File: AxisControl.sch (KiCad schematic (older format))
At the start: 0 parts

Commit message: Added the rest of the printer parts. Should be complete more or less.
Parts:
- added J5: Max, symbol Connector_Generic:Conn_02x01
- added J6: Min, symbol Connector_Generic:Conn_02x01
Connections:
- new net GND: J5.2 (Pin_2), J6.2 (Pin_2)
- new net MaxStop/SENSOR: J5.1 (Pin_1)
- new net MinStop/SENSOR: J6.1 (Pin_1)
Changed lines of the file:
@@
 EESchema Schematic File Version 4
+LIBS:PrntrBoardV1-cache
 EELAYER 26 0
 EELAYER END
 $Descr A4 11693 8268
 encoding utf-8
-Sheet 8 29
+Sheet 8 35
 Title ""
 Date ""
@@
 	5150 4000 5150 3300
 Connection ~ 5150 3300
-Text HLabel 6150 3350 2    50   Input ~ 0
-MAXSTOP
 Text HLabel 6150 3500 2    50   Output ~ 0
 MAXSTOP_OUT
 Text HLabel 6150 4150 2    50   Output ~ 0
 MINSTOP_OUT
-Text HLabel 6150 4000 2    50   Input ~ 0
-MINSTOP
-Wire Wire Line
-	6050 4000 6150 4000
 Wire Wire Line
 	6050 4150 6150 4150
 Wire Wire Line
 	6050 3500 6150 3500
-Wire Wire Line
-	6050 3350 6150 3350
+$Comp
+L Connector_Generic:Conn_02x01 J5
+U 1 1 5AE0BB35
+P 6450 3350
+AR Path="/5AC337B6/5ACC0AA2/5AE0BB35" Ref="J5"  Part="1"
+AR Path="/5AC337B6/5ACCA309/5AE0BB35" Ref="J7"  Part="1"
+AR Path="/5AC337B6/5ACE1C6D/5AE0BB35" Ref="J9"  Part="1"
+F 0 "J9" H 6500 3567 50  0000 C CNN
+F 1 "Max" H 6500 3476 50  0000 C CNN
+F 2 "" H 6450 3350 50  0001 C CNN
+F 3 "~" H 6450 3350 50  0001 C CNN
+	1    6450 3350
+	1    0    0    -1
+$EndComp
+$Comp
+L Connector_Generic:Conn_02x01 J6
+U 1 1 5AE0BBC2
+P 6450 4000
+AR Path="/5AC337B6/5ACC0AA2/5AE0BBC2" Ref="J6"  Part="1"
+AR Path="/5AC337B6/5ACCA309/5AE0BBC2" Ref="J8"  Part="1"
+AR Path="/5AC337B6/5ACE1C6D/5AE0BBC2" Ref="J10"  Part="1"
+F 0 "J10" H 6500 4217 50  0000 C CNN
+F 1 "Min" H 6500 4126 50  0000 C CNN
+F 2 "" H 6450 4000 50  0001 C CNN
+F 3 "~" H 6450 4000 50  0001 C CNN
+	1    6450 4000
+	1    0    0    -1
+$EndComp
+$Comp
+L power:GND #PWR013
+U 1 1 5AE0BC50
+P 6850 3400
+AR Path="/5AC337B6/5ACC0AA2/5AE0BC50" Ref="#PWR013"  Part="1"
+AR Path="/5AC337B6/5ACCA309/5AE0BC50" Ref="#PWR024"  Part="1"
+AR Path="/5AC337B6/5ACE1C6D/5AE0BC50" Ref="#PWR035"  Part="1"
+F 0 "#PWR035" H 6850 3150 50  0001 C CNN
+F 1 "GND" H 6855 3227 50  0000 C CNN
+F 2 "" H 6850 3400 50  0001 C CNN
+F 3 "" H 6850 3400 50  0001 C CNN
+	1    6850 3400
+	1    0    0    -1
+$EndComp
+$Comp
+L power:GND #PWR014
+U 1 1 5AE0BC78
+P 6850 4050
+AR Path="/5AC337B6/5ACC0AA2/5AE0BC78" Ref="#PWR014"  Part="1"
+AR Path="/5AC337B6/5ACCA309/5AE0BC78" Ref="#PWR025"  Part="1"
+AR Path="/5AC337B6/5ACE1C6D/5AE0BC78" Ref="#PWR036"  Part="1"
+F 0 "#PWR036" H 6850 3800 50  0001 C CNN
+F 1 "GND" H 6855 3877 50  0000 C CNN
+F 2 "" H 6850 4050 50  0001 C CNN
+F 3 "" H 6850 4050 50  0001 C CNN
+	1    6850 4050
+	1    0    0    -1
+$EndComp
+Wire Wire Line
+	6850 4050 6850 4000
+Wire Wire Line
+	6850 4000 6750 4000
+Wire Wire Line
+	6850 3400 6850 3350
+Wire Wire Line
+	6850 3350 6750 3350
+Wire Wire Line
+	6250 4000 6050 4000
+Wire Wire Line
+	6250 3350 6050 3350
 $EndSCHEMATC

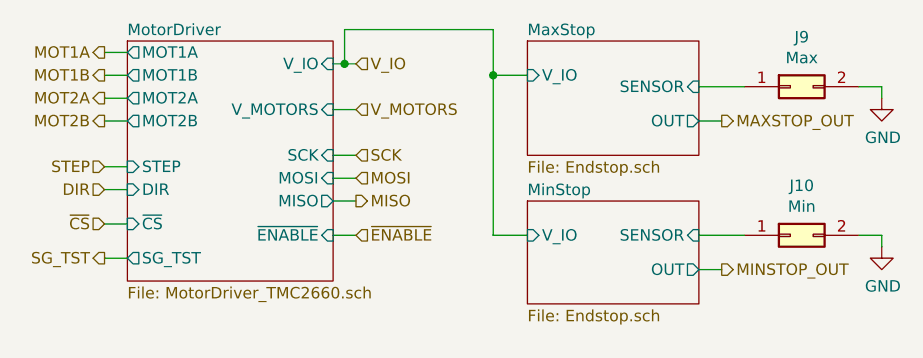
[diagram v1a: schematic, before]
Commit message: Finish the schematics. All pins are assinged to the NUCLEO-64 board.
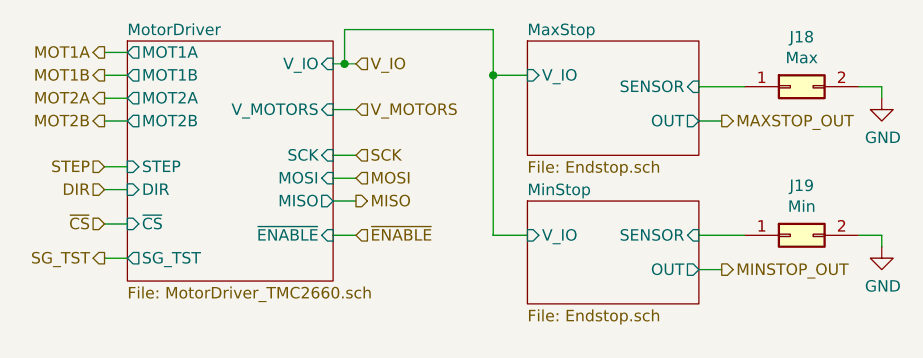
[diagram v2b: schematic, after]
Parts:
- renumbered J5 to J14, J6 to J15
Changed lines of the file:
@@
 	6050 3500 6150 3500
 $Comp
-L Connector_Generic:Conn_02x01 J5
+L Connector_Generic:Conn_02x01 J14
 U 1 1 5AE0BB35
 P 6450 3350
-AR Path="/5AC337B6/5ACC0AA2/5AE0BB35" Ref="J5"  Part="1"
-AR Path="/5AC337B6/5ACCA309/5AE0BB35" Ref="J7"  Part="1"
-AR Path="/5AC337B6/5ACE1C6D/5AE0BB35" Ref="J9"  Part="1"
-F 0 "J9" H 6500 3567 50  0000 C CNN
+AR Path="/5AC337B6/5ACC0AA2/5AE0BB35" Ref="J14"  Part="1"
+AR Path="/5AC337B6/5ACCA309/5AE0BB35" Ref="J16"  Part="1"
+AR Path="/5AC337B6/5ACE1C6D/5AE0BB35" Ref="J18"  Part="1"
+F 0 "J18" H 6500 3567 50  0000 C CNN
 F 1 "Max" H 6500 3476 50  0000 C CNN
 F 2 "" H 6450 3350 50  0001 C CNN
@@
 $EndComp
 $Comp
-L Connector_Generic:Conn_02x01 J6
+L Connector_Generic:Conn_02x01 J15
 U 1 1 5AE0BBC2
 P 6450 4000
-AR Path="/5AC337B6/5ACC0AA2/5AE0BBC2" Ref="J6"  Part="1"
-AR Path="/5AC337B6/5ACCA309/5AE0BBC2" Ref="J8"  Part="1"
-AR Path="/5AC337B6/5ACE1C6D/5AE0BBC2" Ref="J10"  Part="1"
-F 0 "J10" H 6500 4217 50  0000 C CNN
+AR Path="/5AC337B6/5ACC0AA2/5AE0BBC2" Ref="J15"  Part="1"
+AR Path="/5AC337B6/5ACCA309/5AE0BBC2" Ref="J17"  Part="1"
+AR Path="/5AC337B6/5ACE1C6D/5AE0BBC2" Ref="J19"  Part="1"
+F 0 "J19" H 6500 4217 50  0000 C CNN
 F 1 "Min" H 6500 4126 50  0000 C CNN
 F 2 "" H 6450 4000 50  0001 C CNN
@@
 $EndComp
 $Comp
-L power:GND #PWR013
+L power:GND #PWR023
 U 1 1 5AE0BC50
 P 6850 3400
-AR Path="/5AC337B6/5ACC0AA2/5AE0BC50" Ref="#PWR013"  Part="1"
-AR Path="/5AC337B6/5ACCA309/5AE0BC50" Ref="#PWR024"  Part="1"
-AR Path="/5AC337B6/5ACE1C6D/5AE0BC50" Ref="#PWR035"  Part="1"
-F 0 "#PWR035" H 6850 3150 50  0001 C CNN
+AR Path="/5AC337B6/5ACC0AA2/5AE0BC50" Ref="#PWR023"  Part="1"
+AR Path="/5AC337B6/5ACCA309/5AE0BC50" Ref="#PWR034"  Part="1"
+AR Path="/5AC337B6/5ACE1C6D/5AE0BC50" Ref="#PWR045"  Part="1"
+F 0 "#PWR045" H 6850 3150 50  0001 C CNN
 F 1 "GND" H 6855 3227 50  0000 C CNN
 F 2 "" H 6850 3400 50  0001 C CNN
@@
 $EndComp
 $Comp
-L power:GND #PWR014
+L power:GND #PWR024
 U 1 1 5AE0BC78
 P 6850 4050
-AR Path="/5AC337B6/5ACC0AA2/5AE0BC78" Ref="#PWR014"  Part="1"
-AR Path="/5AC337B6/5ACCA309/5AE0BC78" Ref="#PWR025"  Part="1"
-AR Path="/5AC337B6/5ACE1C6D/5AE0BC78" Ref="#PWR036"  Part="1"
-F 0 "#PWR036" H 6850 3800 50  0001 C CNN
+AR Path="/5AC337B6/5ACC0AA2/5AE0BC78" Ref="#PWR024"  Part="1"
+AR Path="/5AC337B6/5ACCA309/5AE0BC78" Ref="#PWR035"  Part="1"
+AR Path="/5AC337B6/5ACE1C6D/5AE0BC78" Ref="#PWR046"  Part="1"
+F 0 "#PWR046" H 6850 3800 50  0001 C CNN
 F 1 "GND" H 6855 3877 50  0000 C CNN
 F 2 "" H 6850 4050 50  0001 C CNN

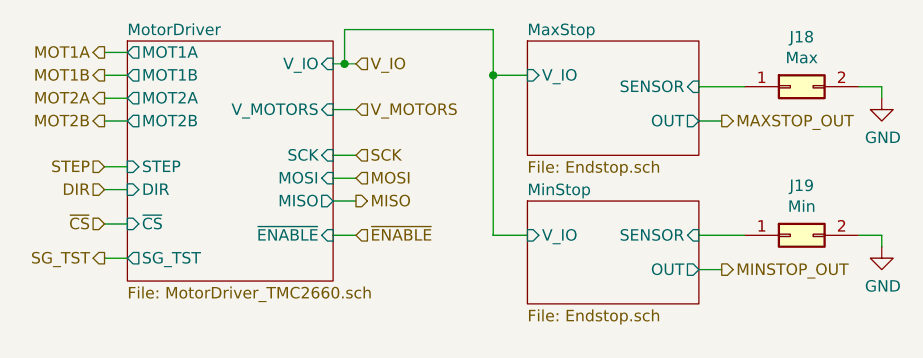
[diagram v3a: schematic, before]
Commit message: Assigned footprints for all components. Inductors are approximate size. MOSFETs dont agree with the footprints. Saved pcb netlist report as report.txt.
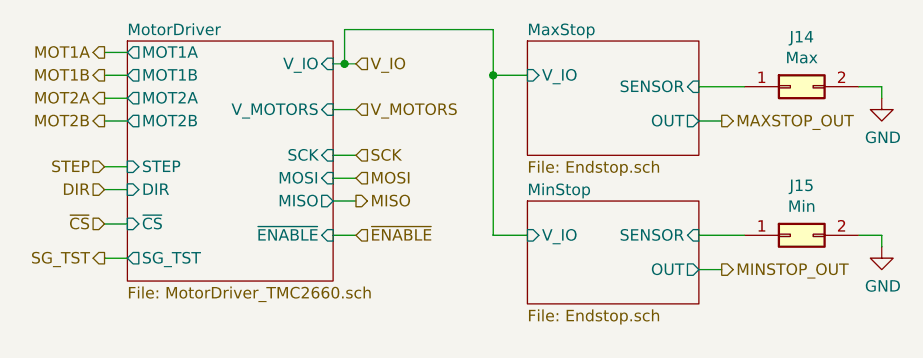
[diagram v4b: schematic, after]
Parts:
- J14, J15: footprint (none) -> Connector_PinHeader_2.54mm:PinHeader_1x02_P2.54mm_Vertical
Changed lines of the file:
@@
 $Descr A4 11693 8268
 encoding utf-8
-Sheet 16 35
+Sheet 8 35
 Title ""
 Date ""
@@
 AR Path="/5AC337B6/5ACCA309/5AE0BB35" Ref="J16"  Part="1"
 AR Path="/5AC337B6/5ACE1C6D/5AE0BB35" Ref="J18"  Part="1"
-F 0 "J18" H 6500 3567 50  0000 C CNN
+F 0 "J14" H 6500 3567 50  0000 C CNN
 F 1 "Max" H 6500 3476 50  0000 C CNN
-F 2 "" H 6450 3350 50  0001 C CNN
+F 2 "Connector_PinHeader_2.54mm:PinHeader_1x02_P2.54mm_Vertical" H 6450 3350 50  0001 C CNN
 F 3 "~" H 6450 3350 50  0001 C CNN
 	1    6450 3350
@@
 AR Path="/5AC337B6/5ACCA309/5AE0BBC2" Ref="J17"  Part="1"
 AR Path="/5AC337B6/5ACE1C6D/5AE0BBC2" Ref="J19"  Part="1"
-F 0 "J19" H 6500 4217 50  0000 C CNN
+F 0 "J15" H 6500 4217 50  0000 C CNN
 F 1 "Min" H 6500 4126 50  0000 C CNN
-F 2 "" H 6450 4000 50  0001 C CNN
+F 2 "Connector_PinHeader_2.54mm:PinHeader_1x02_P2.54mm_Vertical" H 6450 4000 50  0001 C CNN
 F 3 "~" H 6450 4000 50  0001 C CNN
 	1    6450 4000

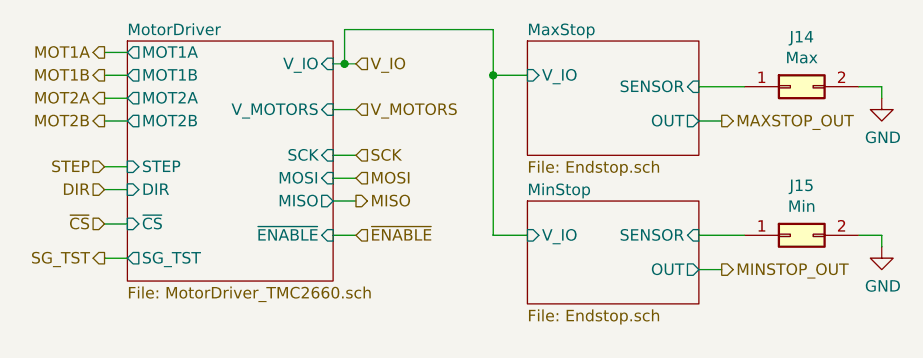
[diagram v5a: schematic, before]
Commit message: Update schematics to use TMC5130/TMC2130 drivers.
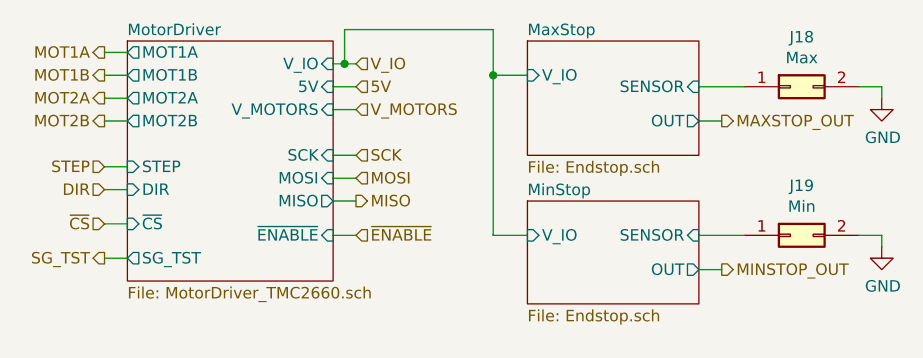
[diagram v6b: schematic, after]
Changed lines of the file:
@@
 F14 "~ENABLE" I R 4450 4000 50
 F15 "SG_TST" O L 3550 4100 50
+F16 "5V" I R 4450 3350 50
 $EndSheet
 Text HLabel 3450 3200 0    50   Output ~ 0
@@
 AR Path="/5AC337B6/5ACCA309/5AE0BB35" Ref="J16"  Part="1"
 AR Path="/5AC337B6/5ACE1C6D/5AE0BB35" Ref="J18"  Part="1"
-F 0 "J14" H 6500 3567 50  0000 C CNN
+F 0 "J18" H 6500 3567 50  0000 C CNN
 F 1 "Max" H 6500 3476 50  0000 C CNN
 F 2 "Connector_PinHeader_2.54mm:PinHeader_1x02_P2.54mm_Vertical" H 6450 3350 50  0001 C CNN
@@
 AR Path="/5AC337B6/5ACCA309/5AE0BBC2" Ref="J17"  Part="1"
 AR Path="/5AC337B6/5ACE1C6D/5AE0BBC2" Ref="J19"  Part="1"
-F 0 "J15" H 6500 4217 50  0000 C CNN
+F 0 "J19" H 6500 4217 50  0000 C CNN
 F 1 "Min" H 6500 4126 50  0000 C CNN
 F 2 "Connector_PinHeader_2.54mm:PinHeader_1x02_P2.54mm_Vertical" H 6450 4000 50  0001 C CNN
@@
 Wire Wire Line
 	6250 3350 6050 3350
+Text HLabel 4550 3350 2    50   Input ~ 0
+5V
+Wire Wire Line
+	4550 3350 4450 3350
 $EndSCHEMATC

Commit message: Added motor clock source.
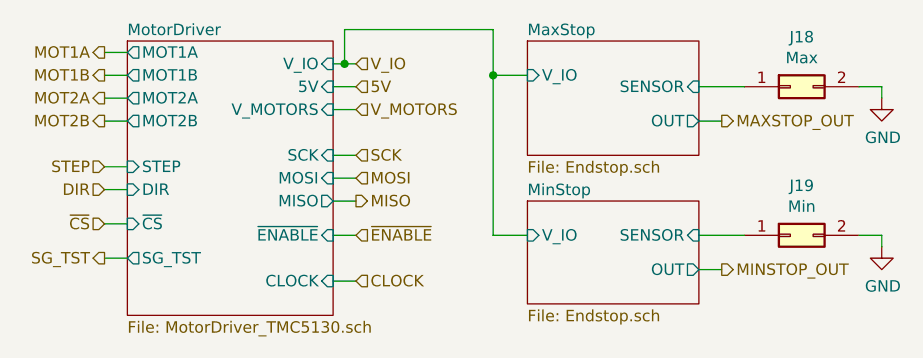
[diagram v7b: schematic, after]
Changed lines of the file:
@@
 $Descr A4 11693 8268
 encoding utf-8
-Sheet 8 34
+Sheet 12 34
 Title ""
 Date ""
@@
 $EndDescr
 $Sheet
-S 3550 3150 900  1050
+S 3550 3150 900  1200
 U 5ACC0B66
 F0 "MotorDriver" 50
-F1 "MotorDriver_TMC2660.sch" 50
+F1 "MotorDriver_TMC5130.sch" 50
 F2 "V_IO" I R 4450 3250 50
 F3 "V_MOTORS" I R 4450 3450 50
@@
 F15 "SG_TST" O L 3550 4100 50
 F16 "5V" I R 4450 3350 50
+F17 "CLOCK" I R 4450 4200 50
 $EndSheet
 Text HLabel 3450 3200 0    50   Output ~ 0
@@
 Wire Wire Line
 	4550 3350 4450 3350
+Text HLabel 4550 4200 2    50   Input ~ 0
+CLOCK
+Wire Wire Line
+	4550 4200 4450 4200
 $EndSCHEMATC

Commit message: Updated motor connector pinout.
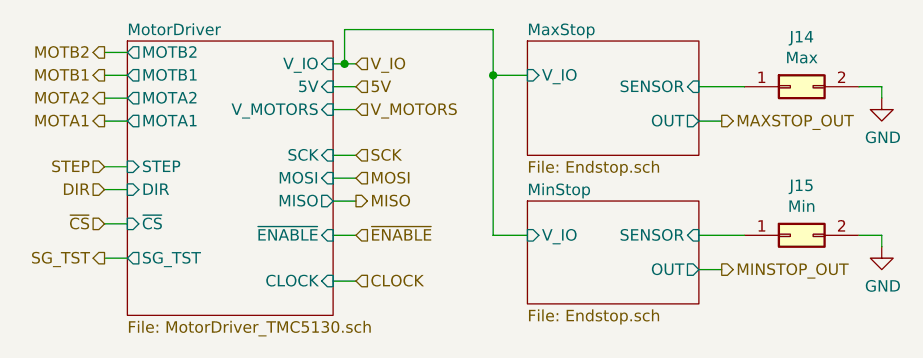
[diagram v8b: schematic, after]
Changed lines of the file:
@@
 $Descr A4 11693 8268
 encoding utf-8
-Sheet 12 34
+Sheet 8 34
 Title ""
 Date ""
@@
 F2 "V_IO" I R 4450 3250 50
 F3 "V_MOTORS" I R 4450 3450 50
-F4 "MOT1B" O L 3550 3300 50
-F5 "MOT1A" O L 3550 3200 50
-F6 "MOT2A" O L 3550 3400 50
-F7 "MOT2B" O L 3550 3500 50
-F8 "STEP" I L 3550 3700 50
-F9 "DIR" I L 3550 3800 50
-F10 "~CS" I L 3550 3950 50
-F11 "SCK" I R 4450 3650 50
-F12 "MOSI" I R 4450 3750 50
-F13 "MISO" O R 4450 3850 50
-F14 "~ENABLE" I R 4450 4000 50
-F15 "SG_TST" O L 3550 4100 50
-F16 "5V" I R 4450 3350 50
-F17 "CLOCK" I R 4450 4200 50
+F4 "STEP" I L 3550 3700 50
+F5 "DIR" I L 3550 3800 50
+F6 "~CS" I L 3550 3950 50
+F7 "SCK" I R 4450 3650 50
+F8 "MOSI" I R 4450 3750 50
+F9 "MISO" O R 4450 3850 50
+F10 "~ENABLE" I R 4450 4000 50
+F11 "SG_TST" O L 3550 4100 50
+F12 "5V" I R 4450 3350 50
+F13 "CLOCK" I R 4450 4200 50
+F14 "MOTB1" O L 3550 3300 50
+F15 "MOTA1" O L 3550 3500 50
+F16 "MOTA2" O L 3550 3400 50
+F17 "MOTB2" O L 3550 3200 50
 $EndSheet
+Text HLabel 3450 3500 0    50   Output ~ 0
+MOTA1
+Text HLabel 3450 3300 0    50   Output ~ 0
+MOTB1
+Text HLabel 3450 3400 0    50   Output ~ 0
+MOTA2
 Text HLabel 3450 3200 0    50   Output ~ 0
-MOT1A
-Text HLabel 3450 3300 0    50   Output ~ 0
-MOT1B
-Text HLabel 3450 3400 0    50   Output ~ 0
-MOT2A
-Text HLabel 3450 3500 0    50   Output ~ 0
-MOT2B
+MOTB2
 Text HLabel 3450 3700 0    50   Input ~ 0
 STEP
@@
 AR Path="/5AC337B6/5ACCA309/5AE0BB35" Ref="J16"  Part="1"
 AR Path="/5AC337B6/5ACE1C6D/5AE0BB35" Ref="J18"  Part="1"
-F 0 "J18" H 6500 3567 50  0000 C CNN
+F 0 "J14" H 6500 3567 50  0000 C CNN
 F 1 "Max" H 6500 3476 50  0000 C CNN
 F 2 "Connector_PinHeader_2.54mm:PinHeader_1x02_P2.54mm_Vertical" H 6450 3350 50  0001 C CNN
@@
 AR Path="/5AC337B6/5ACCA309/5AE0BBC2" Ref="J17"  Part="1"
 AR Path="/5AC337B6/5ACE1C6D/5AE0BBC2" Ref="J19"  Part="1"
-F 0 "J19" H 6500 4217 50  0000 C CNN
+F 0 "J15" H 6500 4217 50  0000 C CNN
 F 1 "Min" H 6500 4126 50  0000 C CNN
 F 2 "Connector_PinHeader_2.54mm:PinHeader_1x02_P2.54mm_Vertical" H 6450 4000 50  0001 C CNN
